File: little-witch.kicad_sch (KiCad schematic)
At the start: 31 parts, among them J1 GCT-USB4105, J3 Conn_ARM_SWD_TagConnect_TC203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, J4 GCT-USB4105, J5 Conn_02x20_Odd_Even, J6 BOOT0_SEL, SW1 SW_Push, U1 CH32V307RCT6, Y1 SIT8008BI-73-33N-25.000000

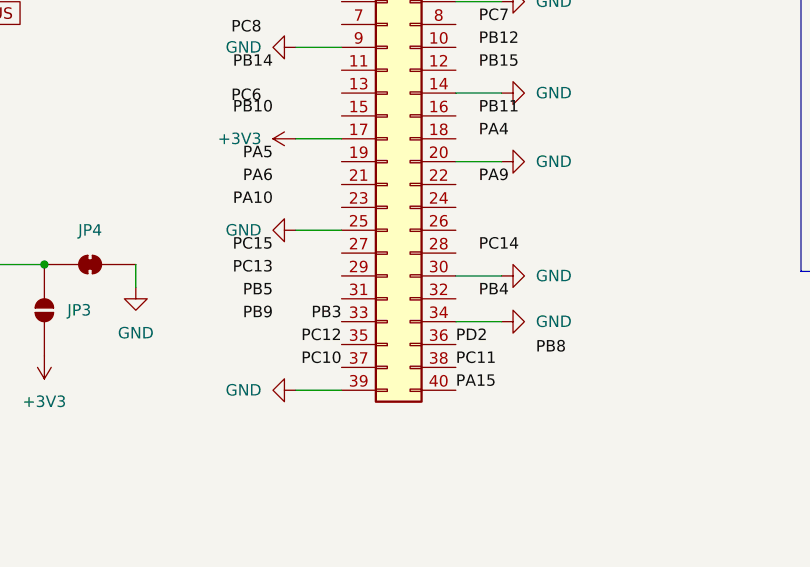
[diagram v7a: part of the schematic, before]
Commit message: GPIO routing
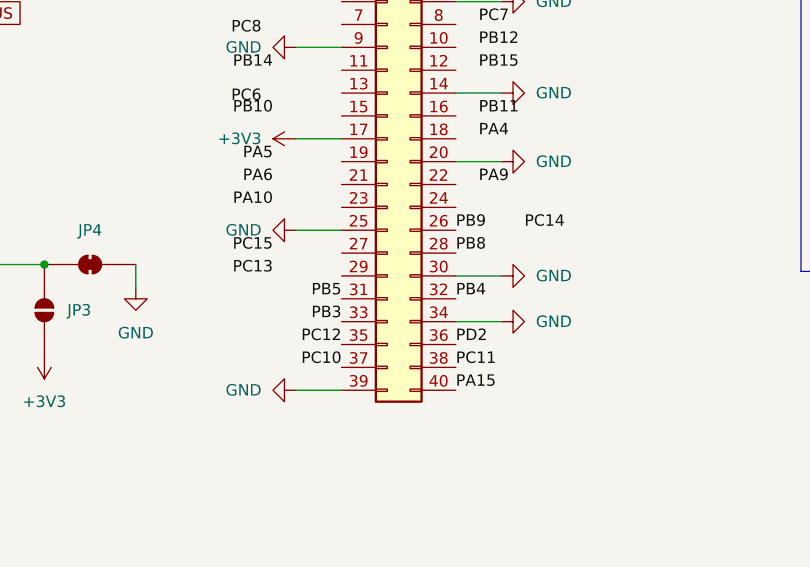
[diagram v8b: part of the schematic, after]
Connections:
- net PB4: now also J5.32 (Pin_32)
- net PB5: now also J5.31 (Pin_31)
- net PB8: now also J5.28 (Pin_28)
- net PB9: now also J5.26 (Pin_26)
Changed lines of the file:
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@@
 	)
 	(label "PC14"
-		(at 185.42 137.16 0)
+		(at 190.5 134.62 0)
 		(effects
 			(font
@@
 	)
 	(label "PB8"
-		(at 191.77 148.59 0)
+		(at 182.88 137.16 0)
 		(effects
 			(font
@@
 		)
 	)
-	(label "PB9"
-		(at 162.56 144.78 180)
-		(effects
-			(font
-				(size 1.27 1.27)
-			)
-			(justify right bottom)
-		)
-	)
 	(label "PB12"
 		(at 185.42 114.3 0)
@@
 	)
 	(label "PB4"
-		(at 185.42 142.24 0)
+		(at 182.88 142.24 0)
 		(effects
 			(font
@@
 		)
 	)
+	(label "PB9"
+		(at 182.88 134.62 0)
+		(effects
+			(font
+				(size 1.27 1.27)
+			)
+			(justify left bottom)
+		)
+	)
 	(label "PB11"
 		(at 185.42 121.92 0)
@@
 	)
 	(label "PB5"
-		(at 162.56 142.24 180)
-		(effects
-			(font
+		(at 170.18 142.24 180)
+		(effects
+			(font
